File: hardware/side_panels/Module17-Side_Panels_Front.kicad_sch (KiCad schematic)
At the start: 2 parts

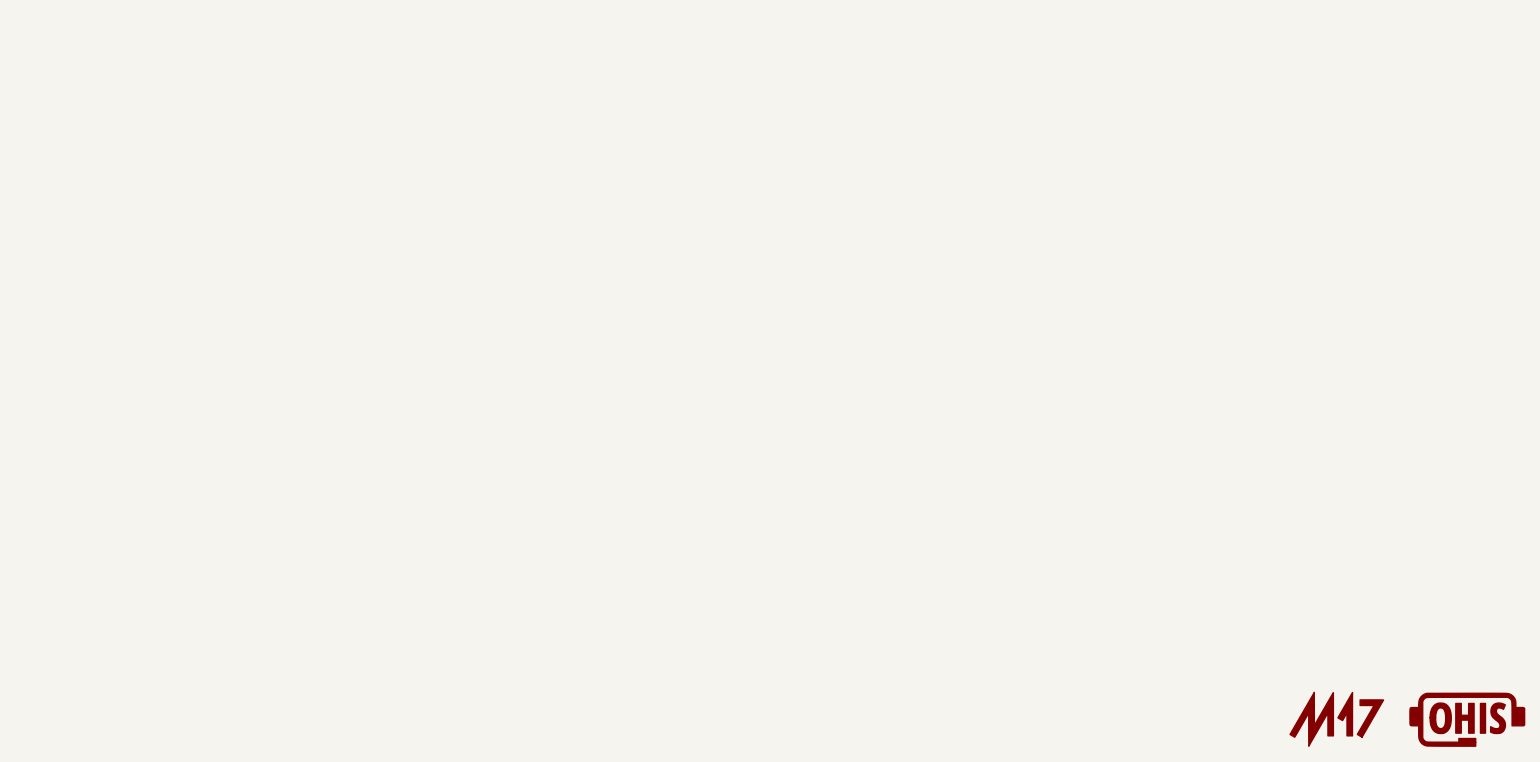
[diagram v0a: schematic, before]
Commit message: Updated HMI side panels
Increased text size, added holes for the corners, added schematic title bloc plus misc. changes
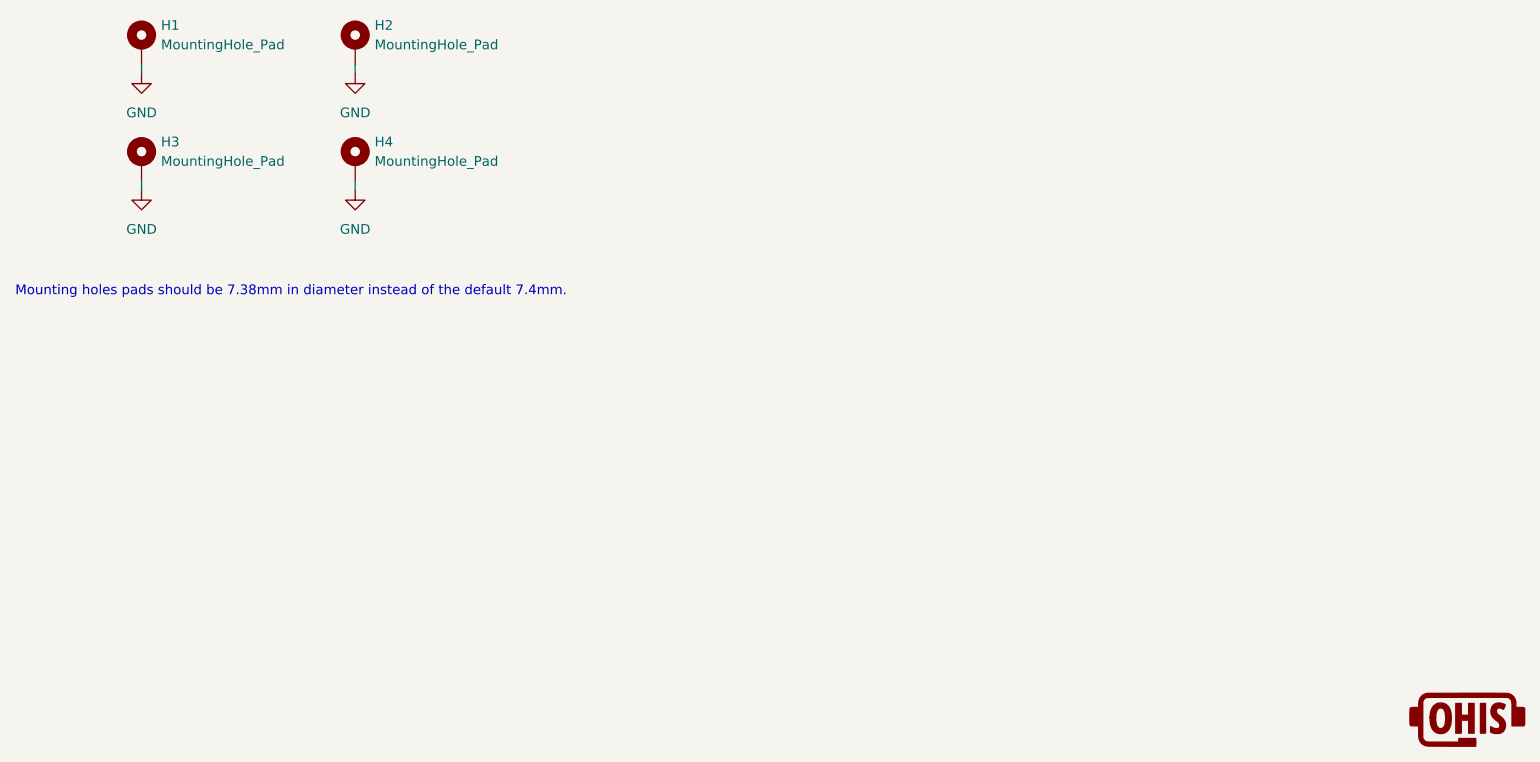
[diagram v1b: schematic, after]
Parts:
- removed LOGO1: M17_logo, M17_logos:M17_logo_20x11.5mm, symbol M17_logos:M17_logo
- added H1, H2, H3, H4: MountingHole_Pad, MountingHole:MountingHole_3.7mm_Pad_Via, symbol Mechanical:MountingHole_Pad
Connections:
- new net GND: H1.1, H2.1, H3.1, H4.1
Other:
- note added: "Mounting holes pads should be 7.38mm in diameter instead of the default 7.4mm."
- title: (none) -> Module17 HMI Back Panel
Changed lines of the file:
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@@
 (kicad_sch (version 20230121) (generator eeschema)
   (paper "A4")
+  (title_block
+    (title "Module17 HMI Back Panel")
+    (date "2024-01-11")
+    (rev "Rev 0.99")
+    (comment 1 "Morgan ON4MOD")
+  )
+  (wire (pts (xy 100.33 102.87) (xy 100.33 104.14))
+    (stroke (width 0) (type default))
+  )
+  (wire (pts (xy 128.27 87.63) (xy 128.27 88.9))
+    (stroke (width 0) (type default))
+  )
+  (wire (pts (xy 100.33 87.63) (xy 100.33 88.9))
+    (stroke (width 0) (type default))
+  )
+  (wire (pts (xy 128.27 102.87) (xy 128.27 104.14))
+    (stroke (width 0) (type default))
+  )
+  (text "Mounting holes pads should be 7.38mm in diameter instead of the default 7.4mm."
+    (at 83.82 118.11 0)
+    (effects (font (size 1.27 1.27)) (justify left bottom))
+  )
+  (symbol (lib_id "Mechanical:MountingHole_Pad") (at 100.33 100.33 0) (unit 1)
+    (in_bom yes) (on_board yes) (dnp no)
+    (property "Reference" "H3" (at 102.87 97.79 0)
+      (effects (font (size 1.27 1.27)) (justify left))
+    )
+    (property "Value" "MountingHole_Pad" (at 102.87 100.33 0)
+      (effects (font (size 1.27 1.27)) (justify left))
+    )
+    (property "Footprint" "MountingHole:MountingHole_3.7mm_Pad_Via" (at 100.33 100.33 0)
+      (effects (font (size 1.27 1.27)) hide)
+    )
+    (property "Datasheet" "~" (at 100.33 100.33 0)
+      (effects (font (size 1.27 1.27)) hide)
+    )
+    (pin "1")
+    (instances
+      (project "Module17-Side_Panels_Front"
+        (path "/781e5e3e-5d0e-465e-be6a-c37775f661bf"
+          (reference "H3") (unit 1)
+        )
+      )
+    )
+  )
+  (symbol (lib_id "Mechanical:MountingHole_Pad") (at 100.33 85.09 0) (unit 1)
+    (in_bom yes) (on_board yes) (dnp no) (fields_autoplaced)
+    (property "Reference" "H1" (at 102.87 82.55 0)
+      (effects (font (size 1.27 1.27)) (justify left))
+    )
+    (property "Value" "MountingHole_Pad" (at 102.87 85.09 0)
+      (effects (font (size 1.27 1.27)) (justify left))
+    )
+    (property "Footprint" "MountingHole:MountingHole_3.7mm_Pad_Via" (at 100.33 85.09 0)
+      (effects (font (size 1.27 1.27)) hide)
+    )
+    (property "Datasheet" "~" (at 100.33 85.09 0)
+      (effects (font (size 1.27 1.27)) hide)
+    )
+    (pin "1")
+    (instances
+      (project "Module17-Side_Panels_Front"
+        (path "/781e5e3e-5d0e-465e-be6a-c37775f661bf"
+          (reference "H1") (unit 1)
+        )
+      )
+    )
+  )
+  (symbol (lib_id "Mechanical:MountingHole_Pad") (at 128.27 100.33 0) (unit 1)
+    (in_bom yes) (on_board yes) (dnp no) (fields_autoplaced)
+    (property "Reference" "H4" (at 130.81 97.79 0)
+      (effects (font (size 1.27 1.27)) (justify left))
+    )
+    (property "Value" "MountingHole_Pad" (at 130.81 100.33 0)
+      (effects (font (size 1.27 1.27)) (justify left))
+    )
+    (property "Footprint" "MountingHole:MountingHole_3.7mm_Pad_Via" (at 128.27 100.33 0)
+      (effects (font (size 1.27 1.27)) hide)
+    )
+    (property "Datasheet" "~" (at 128.27 100.33 0)
+      (effects (font (size 1.27 1.27)) hide)
+    )
+    (pin "1")
+    (instances
+      (project "Module17-Side_Panels_Front"
+        (path "/781e5e3e-5d0e-465e-be6a-c37775f661bf"
+          (reference "H4") (unit 1)
+        )
+      )
+    )
+  )
+  (symbol (lib_id "power:GND") (at 128.27 88.9 0) (unit 1)
+    (in_bom yes) (on_board yes) (dnp no) (fields_autoplaced)
+    (property "Reference" "#PWR02" (at 128.27 95.25 0)
+      (effects (font (size 1.27 1.27)) hide)
+    )
+    (property "Value" "GND" (at 128.27 93.98 0)
+      (effects (font (size 1.27 1.27)))
+    )
+    (property "Footprint" "" (at 128.27 88.9 0)
+      (effects (font (size 1.27 1.27)) hide)
+    )
+    (property "Datasheet" "" (at 128.27 88.9 0)
+      (effects (font (size 1.27 1.27)) hide)
+    )
+    (pin "1")
+    (instances
+      (project "Module17-Side_Panels_Front"
+        (path "/781e5e3e-5d0e-465e-be6a-c37775f661bf"
+          (reference "#PWR02") (unit 1)
+        )
+      )
+    )
+  )
+  (symbol (lib_id "power:GND") (at 128.27 104.14 0) (unit 1)
+    (in_bom yes) (on_board yes) (dnp no) (fields_autoplaced)
+    (property "Reference" "#PWR04" (at 128.27 110.49 0)
+      (effects (font (size 1.27 1.27)) hide)
+    )
+    (property "Value" "GND" (at 128.27 109.22 0)
+      (effects (font (size 1.27 1.27)))
+    )
+    (property "Footprint" "" (at 128.27 104.14 0)
+      (effects (font (size 1.27 1.27)) hide)
+    )
+    (property "Datasheet" "" (at 128.27 104.14 0)
+      (effects (font (size 1.27 1.27)) hide)
+    )
+    (pin "1")
+    (instances
+      (project "Module17-Side_Panels_Front"
+        (path "/781e5e3e-5d0e-465e-be6a-c37775f661bf"
+          (reference "#PWR04") (unit 1)
+        )
+      )
+    )
+  )
+  (symbol (lib_id "power:GND") (at 100.33 104.14 0) (unit 1)
+    (in_bom yes) (on_board yes) (dnp no) (fields_autoplaced)
+    (property "Reference" "#PWR03" (at 100.33 110.49 0)
+      (effects (font (size 1.27 1.27)) hide)
+    )
+    (property "Value" "GND" (at 100.33 109.22 0)
+      (effects (font (size 1.27 1.27)))
+    )
+    (property "Footprint" "" (at 100.33 104.14 0)
+      (effects (font (size 1.27 1.27)) hide)
+    )
+    (property "Datasheet" "" (at 100.33 104.14 0)
+      (effects (font (size 1.27 1.27)) hide)
+    )
+    (pin "1")
+    (instances
+      (project "Module17-Side_Panels_Front"
+        (path "/781e5e3e-5d0e-465e-be6a-c37775f661bf"
+          (reference "#PWR03") (unit 1)
+        )
+      )
+    )
+  )
   (symbol (lib_id "M17_logos:OHIS_logo") (at 273.685 173.355 0) (unit 1)
     (in_bom yes) (on_board yes) (dnp no) (fields_autoplaced)
@@
     )
     (instances
-      (project "side_panels"
+      (project "Module17-Side_Panels_Front"
         (path "/781e5e3e-5d0e-465e-be6a-c37775f661bf"
           (reference "LOGO2") (unit 1)
@@
     )
   )
-  (symbol (lib_id "M17_logos:M17_logo") (at 256.54 173.355 0) (unit 1)
-    (in_bom no) (on_board yes) (dnp no) (fields_autoplaced)
-    (property "Reference" "LOGO1" (at 256.54 168.529 0)
-      (effects (font (size 1.27 1.27)) hide)
-    )
-    (property "Value" "M17_logo" (at 256.54 168.402 0)
-      (effects (font (size 1.27 1.27)) hide)
-    )
-    (property "Footprint" "M17_logos:M17_logo_20x11.5mm" (at 253.365 171.069 0)
-      (effects (font (size 1.27 1.27)) hide)
-    )
-    (property "Datasheet" "" (at 253.365 171.069 0)
-      (effects (font (size 1.27 1.27)) hide)
-    )
-    (instances
-      (project "side_panels"
-        (path "/781e5e3e-5d0e-465e-be6a-c37775f661bf"
-          (reference "LOGO1") (unit 1)
-        )
-      )
+  (symbol (lib_id "Mechanical:MountingHole_Pad") (at 128.27 85.09 0) (unit 1)
+    (in_bom yes) (on_board yes) (dnp no) (fields_autoplaced)
+    (property "Reference" "H2" (at 130.81 82.55 0)
+      (effects (font (size 1.27 1.27)) (justify left))
+    )
+    (property "Value" "MountingHole_Pad" (at 130.81 85.09 0)
+      (effects (font (size 1.27 1.27)) (justify left))
+    )
+    (property "Footprint" "MountingHole:MountingHole_3.7mm_Pad_Via" (at 128.27 85.09 0)
+      (effects (font (size 1.27 1.27)) hide)
+    )
+    (property "Datasheet" "~" (at 128.27 85.09 0)
+      (effects (font (size 1.27 1.27)) hide)
+    )
+    (pin "1")
+    (instances
+      (project "Module17-Side_Panels_Front"
+        (path "/781e5e3e-5d0e-465e-be6a-c37775f661bf"
+          (reference "H2") (unit 1)
+        )
+      )
+    )
+  )
+  (symbol (lib_id "power:GND") (at 100.33 88.9 0) (unit 1)
+    (in_bom yes) (on_board yes) (dnp no) (fields_autoplaced)
+    (property "Reference" "#PWR01" (at 100.33 95.25 0)
+      (effects (font (size 1.27 1.27)) hide)
+    )
+    (property "Value" "GND" (at 100.33 93.98 0)
+      (effects (font (size 1.27 1.27)))
+    )
+    (property "Footprint" "" (at 100.33 88.9 0)
+      (effects (font (size 1.27 1.27)) hide)
+    )
+    (property "Datasheet" "" (at 100.33 88.9 0)
+      (effects (font (size 1.27 1.27)) hide)
+    )
+    (pin "1")
+    (instances
+      (project "Module17-Side_Panels_Front"
+        (path "/781e5e3e-5d0e-465e-be6a-c37775f661bf"
+          (reference "#PWR01") (unit 1)
+        )
+      )

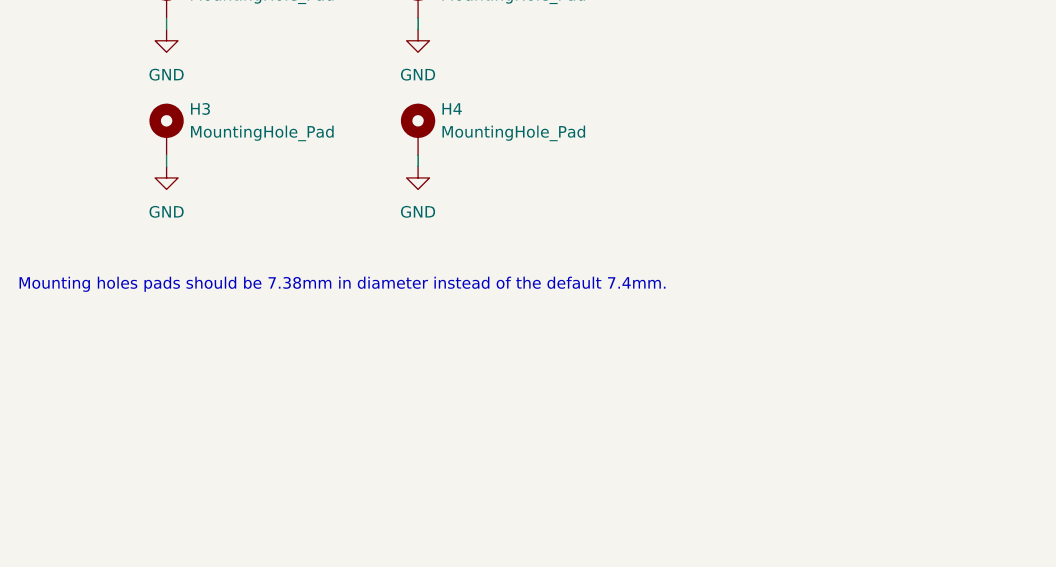
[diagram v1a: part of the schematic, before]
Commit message: Updated Side Panels to Rev 0.99b
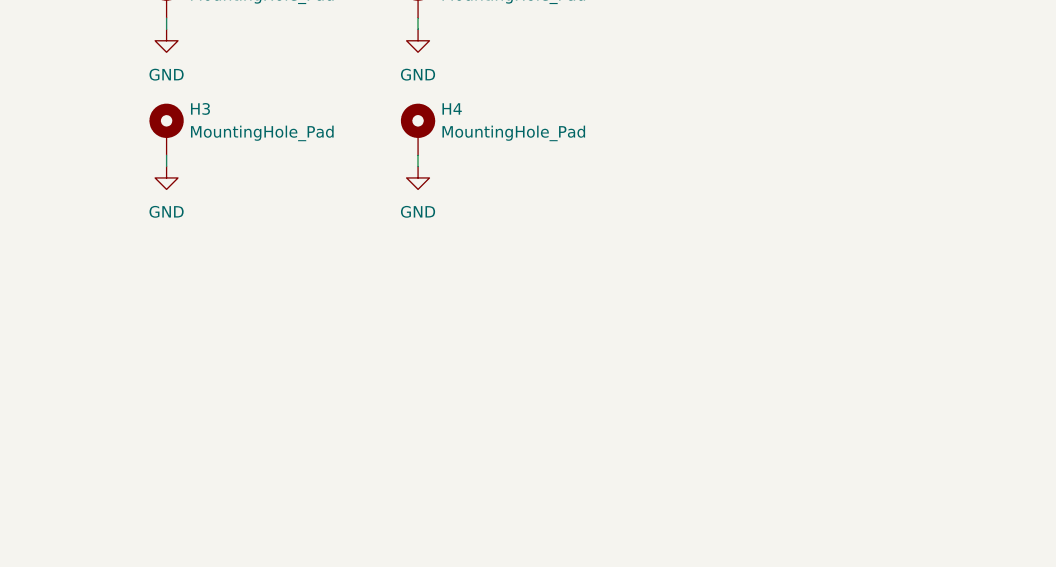
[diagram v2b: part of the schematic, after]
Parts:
- H1, H2, H3, H4: footprint MountingHole:MountingHole_3.7mm_Pad_Via -> M17_mounting_hole:MountingHole_3.7mm_Pad_Via_Small_Pad
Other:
- note removed: "Mounting holes pads should be 7.38mm in diameter instead of the default 7.4mm."

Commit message: Updated side panels PCBs to revision 1.0
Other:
- company: (none) -> M17 Project
- title: Module17 HMI Back Panel -> Module17 HMI Front Panel
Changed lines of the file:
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@@
 	(paper "A4")
 	(title_block
-		(title "Module17 HMI Back Panel")
-		(date "2024-01-11")
-		(rev "Rev 0.99")
+		(title "Module17 HMI Front Panel")
+		(date "2024-06-19")
+		(rev "Rev 1.0")
+		(company "M17 Project")
 		(comment 1 "Morgan ON4MOD")
+		(comment 2 "Authors:")
 	)
 	(wire
